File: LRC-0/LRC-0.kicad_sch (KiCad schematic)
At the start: 57 parts, among them J1 USB_C_Receptacle_USB2.0_14P, J2 Battery, J3 SMA, J4 u.FL, J5 Conn_01x08, SW1 EN, SW2 BOOT, U2 AP7361C-33E, U3 TVS1400DRV, U4 BQ24075RGT, U5 ESP32-C6-MINI-1, U6 SX1262IMLTRT, U7 BGS12WN6E6327, U8 BGS12WN6E6327, Y1 TX32-33015S-32.000-X-R

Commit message: most footprints + new rf switch (lowkey might switch back), peripherals
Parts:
- removed J5: Conn_01x08, symbol Connector_Generic:Conn_01x08
- removed U7, U8: BGS12WN6E6327, Package_LGA:Infineon_PG-TSNP-6-10_0.7x1.1mm_0.7x1.1mm_P0.4mm, symbol RF_Switch:BGS12WN6E6327
- added C22, C23: 100n, Capacitor_SMD:C_0402_1005Metric, symbol Device:C
- added J5: SPI Display, Connector_PinHeader_2.54mm:PinHeader_1x04_P2.54mm_Vertical, symbol Connector_Generic:Conn_01x04
- added R10, R17, R18, R19: 10k, Resistor_SMD:R_0402_1005Metric, symbol Device:R
- added SW3: RotaryEncoder, symbol Device:RotaryEncoder
- added SW4: 1, Button_Switch_SMD:SW_Push_SPST_NO_Alps_SKRK, symbol Switch:SW_Push
- added SW5: 0, Button_Switch_SMD:SW_Push_SPST_NO_Alps_SKRK, symbol Switch:SW_Push
- added U1, U8: RFSW1012TR7, Package_DFN_QFN:LQFN-12-1EP_2x2mm_P0.5mm_EP0.7x0.7mm, symbol RFSW1012:RFSW1012TR7
- C16: value 1u -> 470n
- C19, C20, C21: footprint (none) -> Capacitor_SMD:C_0402_1005Metric
- J1: footprint (none) -> Connector_USB:USB_C_Receptacle_GCT_USB4105-xx-A_16P_TopMnt_Horizontal
- J2: footprint (none) -> Connector_PinHeader_2.54mm:PinHeader_1x02_P2.54mm_Vertical
- J3: footprint (none) -> Connector_Coaxial:SMA_Amphenol_132289_EdgeMount
- J4: footprint (none) -> Connector_Coaxial:U.FL_Hirose_U.FL-R-SMT-1_Vertical
- R16: footprint (none) -> Resistor_SMD:R_0402_1005Metric
- SW1, SW2: footprint (none) -> Button_Switch_SMD:SW_Push_SPST_NO_Alps_SKRK
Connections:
- net +3V3: now also R10.1, R17.1, R18.1, R19.1, U1.9 (VDD), U8.9 (VDD)
- net ANT1: now also U8.5 (RF1)
- net ANT2: now also U8.11 (RF2)
- net ANT_CTRL: now also U8.7 (CTRL)
- net GND: now also C22.2, C23.2, SW4.2, SW5.2, U1.1 (GND), U1.10 (GND), U1.12 (GND), U1.3 (GND), U1.4 (GND), U1.6 (GND), U8.1 (GND), U8.10 (GND), U8.12 (GND), U8.3 (GND), U8.4 (GND), U8.6 (GND)
- net IO0: now also J5.1 (Pin_1)
- net IO1: now also J5.2 (Pin_2)
- net IO2: now also J5.3 (Pin_3)
- net IO3: now also J5.4 (Pin_4)
- net IO4: now also SW3.A
- net IO5: now also SW3.C
- net IO6: now also SW3.B
- net IO7: now also C23.1, R19.2, SW4.1
- net IO8: now also C22.1, R18.2, SW5.1
- net RF1: now also U1.5 (RF1)
- net RF2: now also U1.11 (RF2)
- net RFIN_A: now also U8.2 (RFC)
- net at R16.2: now also U1.7 (CTRL)
- net at C19.2: now also U1.2 (RFC)
- new net: R17.2, U8.8 (EN)
- new net: R10.2, U1.8 (EN)
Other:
- note removed: "GPIO"
- moved on the sheet: C19, C20, C21, FL1, J3, J4, R16

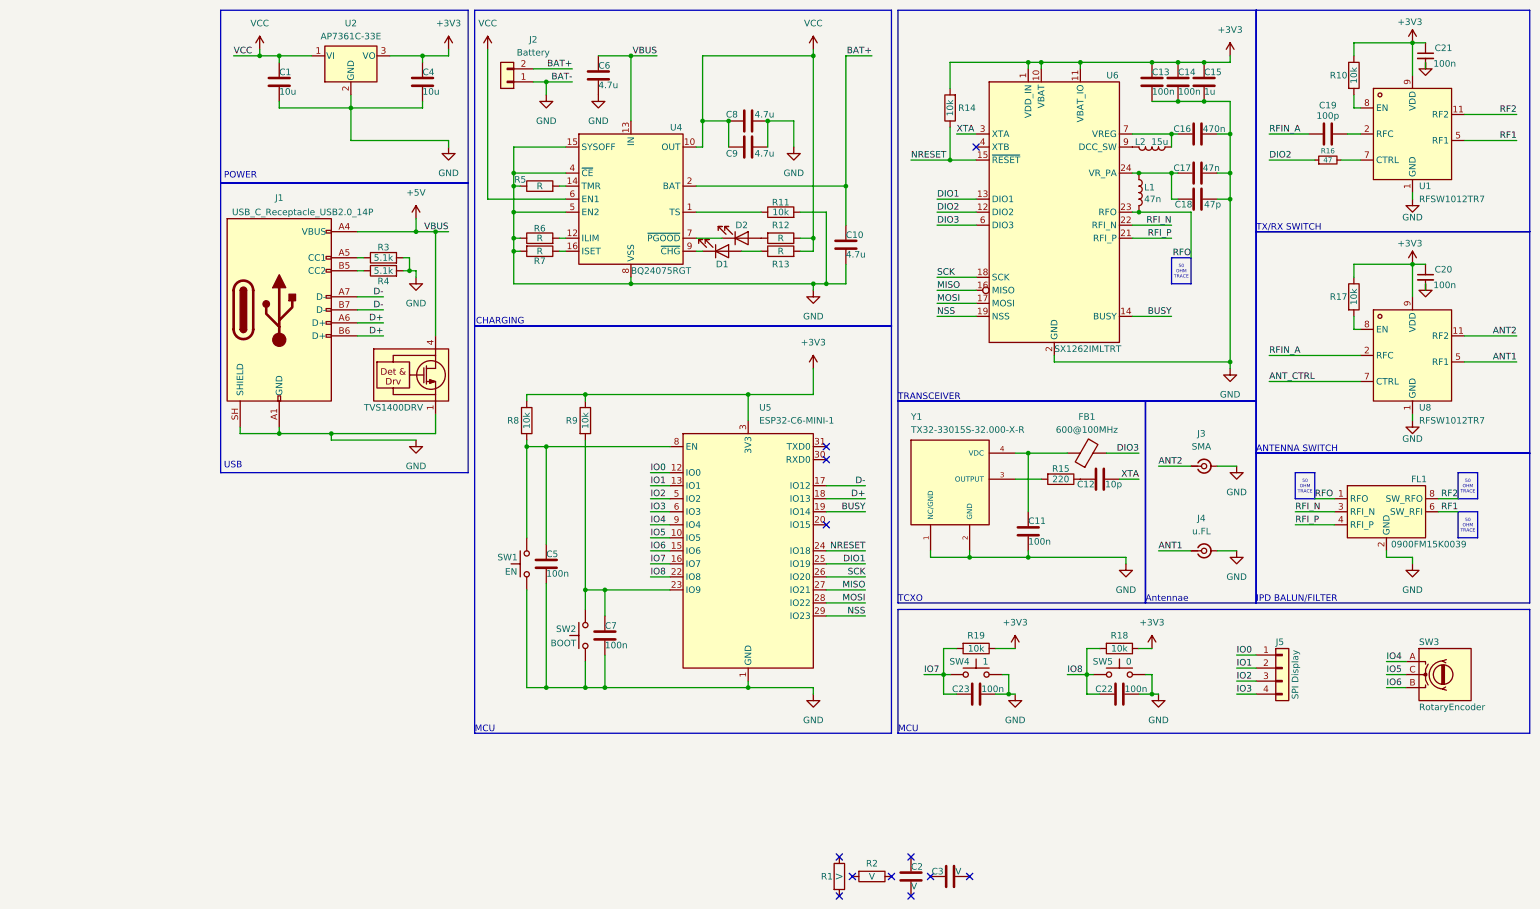
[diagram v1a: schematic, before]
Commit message: battery charger ic fix + peripherals
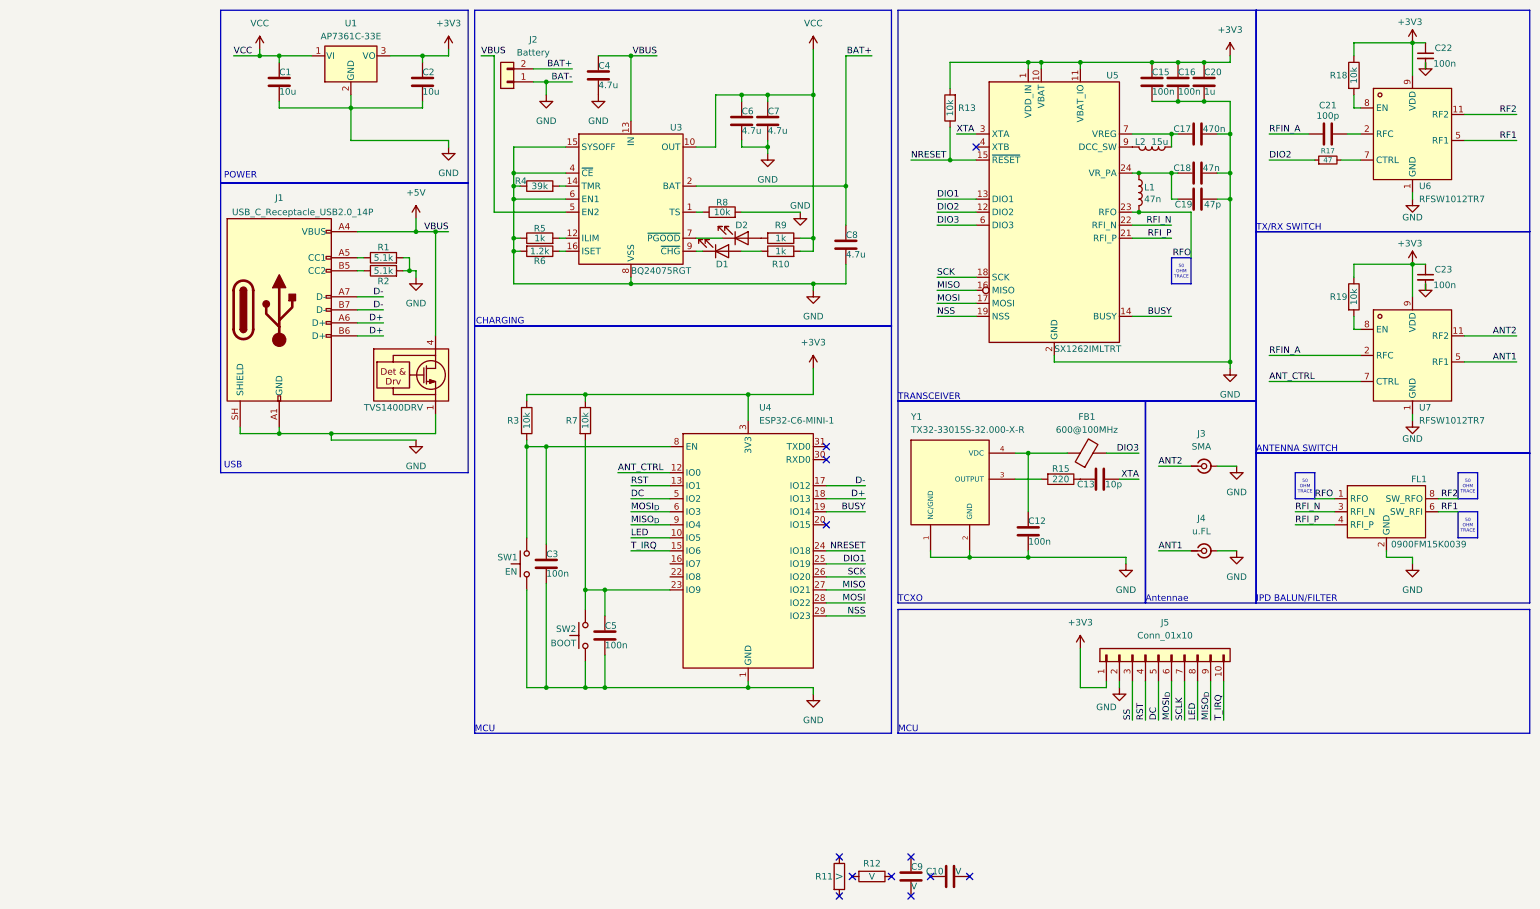
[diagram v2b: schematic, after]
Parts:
- removed C22, C23: 100n, Capacitor_SMD:C_0402_1005Metric, symbol Device:C
- removed C8, C9: 4.7u, Capacitor_SMD:C_0402_1005Metric, symbol Device:C
- removed J5: SPI Display, Connector_PinHeader_2.54mm:PinHeader_1x04_P2.54mm_Vertical, symbol Connector_Generic:Conn_01x04
- removed R11, R18, R19: 10k, Resistor_SMD:R_0402_1005Metric, symbol Device:R
- removed R5: R, Resistor_SMD:R_0402_1005Metric, symbol Device:R
- removed SW3: RotaryEncoder, symbol Device:RotaryEncoder
- removed SW4: 1, Button_Switch_SMD:SW_Push_SPST_NO_Alps_SKRK, symbol Switch:SW_Push
- removed SW5: 0, Button_Switch_SMD:SW_Push_SPST_NO_Alps_SKRK, symbol Switch:SW_Push
- added C6, C7: 4.7u, Capacitor_SMD:C_0402_1005Metric, symbol Device:C
- added J5: Conn_01x10, symbol Connector_Generic:Conn_01x10
- added R4: 39k, Resistor_SMD:R_0402_1005Metric, symbol Device:R
- added R8: 10k, Resistor_SMD:R_0402_1005Metric, symbol Device:R
- R10: renamed from R13; value R -> 1k
- R5: renamed from R6; value R -> 1k
- R6: renamed from R7; value R -> 1.2k
- R9: renamed from R12; value R -> 1k
- U4: renamed from U5; footprint RF_Module:ESP32-C6-MINI-1 -> RF_Module:ESP32-S3-WROOM-1
- renumbered C3 to C10, C11 to C12, C12 to C13, C13 to C15, C14 to C16, C16 to C17, C17 to C18, C18 to C19, C4 to C2, C15 to C20, C19 to C21, C21 to C22, C20 to C23, C5 to C3, C6 to C4, C7 to C5, C10 to C8, C2 to C9, R3 to R1, R1 to R11, R2 to R12, R14 to R13, R16 to R17, R10 to R18, R17 to R19, R4 to R2, R8 to R3, R9 to R7, U2 to U1, U3 to U2, U4 to U3, U6 to U5, U1 to U6, U8 to U7
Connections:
- net IO0 is gone; now on net ANT_CTRL: U4.12 (IO0)
- net +3V3: now also J5.1 (Pin_1)
- net +5V: now also U3.5 (EN2)
- net GND: now also U3.6 (EN1), C6.2, C7.2, J5.2 (Pin_2), R4.1, R8.2; no longer U3.5 (EN2)
- net VCC: now also C6.1, C7.1; no longer U3.6 (EN1)
- net at U3.1 (TS): now also R8.1
- net at U3.14 (TMR): now also R4.2
- net IO1 renamed RST
- net RST: now also J5.4 (Pin_4)
- net IO2 renamed DC
- net DC: now also J5.5 (Pin_5)
- net IO3 renamed MOSI_{D}
- net MOSI_{D}: now also J5.6 (Pin_6)
- net IO4 renamed MISO_{D}
- net MISO_{D}: now also J5.9 (Pin_9)
- net IO5 renamed LED
- net LED: now also J5.8 (Pin_8)
- net IO6 renamed T_IRQ
- net T_IRQ: now also J5.10 (Pin_10)
- net IO7: no longer names the net of U4.16 (IO7)
- net IO8: no longer names the net of U4.22 (IO8)
- new net SCLK: J5.7 (Pin_7)
- new net SS: J5.3 (Pin_3)

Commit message: schematic
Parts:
- D1, D2: footprint (none) -> LED_SMD:LED_0805_2012Metric
- FB1: footprint (none) -> Inductor_SMD:L_0603_1608Metric
- J5: footprint (none) -> Connector_PinHeader_2.54mm:PinHeader_1x10_P2.54mm_Vertical
- L1, L2: footprint (none) -> Inductor_SMD:L_0402_1005Metric
- U4: footprint RF_Module:ESP32-S3-WROOM-1 -> RF_Module:ESP32-C6-MINI-1
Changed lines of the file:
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@@
 			)
 		)
-		(property "Footprint" ""
+		(property "Footprint" "Inductor_SMD:L_0603_1608Metric"
 			(at 182.88 102.108 90)
 			(hide yes)
@@
 			)
 		)
-		(property "Footprint" "RF_Module:ESP32-S3-WROOM-1"
+		(property "Footprint" "RF_Module:ESP32-C6-MINI-1"
 			(at 134.62 144.78 0)
 			(hide yes)
@@
 			)
 		)
-		(property "Footprint" ""
+		(property "Footprint" "Inductor_SMD:L_0402_1005Metric"
 			(at 193.04 49.53 0)
 			(hide yes)
@@
 			)
 		)
-		(property "Footprint" ""
+		(property "Footprint" "Connector_PinHeader_2.54mm:PinHeader_1x10_P2.54mm_Vertical"
 			(at 196.85 139.7 0)
 			(hide yes)
@@
 			)
 		)
-		(property "Footprint" ""
+		(property "Footprint" "LED_SMD:LED_0805_2012Metric"
 			(at 111.76 60.96 0)
 			(hide yes)
@@
 			)
 		)
-		(property "Footprint" ""
+		(property "Footprint" "LED_SMD:LED_0805_2012Metric"
 			(at 115.57 58.42 0)
 			(hide yes)
@@
 			)
 		)
-		(property "Footprint" ""
+		(property "Footprint" "Inductor_SMD:L_0402_1005Metric"
 			(at 195.58 40.64 0)
 			(hide yes)
@@
 			"8beb553b-cd71-4e2b-a772-223167ccf878" "8e41ce3d-0b87-4755-b8d2-33e1843013d6"
 			"9afd77c0-5f47-4f9b-a946-7a0d697fb9e0" "a762f8ca-3cb3-47ad-83c8-88d4d1871ef0"
-			"b8249c6d-6442-4dcc-b269-77d21086703b" "ba0c39e8-2f22-4ef4-b4bf-0d328bdf618f"
-			"be78885b-46cc-4838-9a52-e03407f3397f" "c0b069ea-f682-487e-baeb-4ab8c4c13c54"
-			"c34ebc55-6302-44df-86b4-516ed0bf5561" "cca19fa7-7724-4027-83f7-f2765abfb53f"
-			"d84ddb03-7766-49f6-835f-c54dc88e8ff7" "dac14064-bced-4c53-b135-80ee0dbc89d7"
-			"dd5d8867-83af-4731-9750-1446e3d6ecbc" "f1fb2587-afb8-41b9-9758-8f391ef28328"
+			"b8249c6d-6442-4dcc-b269-77d21086703b" "be78885b-46cc-4838-9a52-e03407f3397f"
+			"c0b069ea-f682-487e-baeb-4ab8c4c13c54" "c34ebc55-6302-44df-86b4-516ed0bf5561"
+			"cca19fa7-7724-4027-83f7-f2765abfb53f" "d84ddb03-7766-49f6-835f-c54dc88e8ff7"
+			"dac14064-bced-4c53-b135-80ee0dbc89d7" "dd5d8867-83af-4731-9750-1446e3d6ecbc"
+			"f1fb2587-afb8-41b9-9758-8f391ef28328"
 		)
 	)

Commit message: pi filters
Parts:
- added C14, C16, C21, C24, C27: C, Capacitor_SMD:C_0402_1005Metric, symbol Device:C
- added C23: 47n, Capacitor_SMD:C_0402_1005Metric, symbol Device:C
- added L3, L4: L, Inductor_SMD:L_0402_1005Metric, symbol Device:L
- J3: renamed from J5; now not fitted
- renumbered C12 to C11, C13 to C12, C15 to C13, C16 to C15, C21 to C22, C22 to C25, C23 to C26, J3 to J4, J4 to J5, R15 to R14, R17 to R15, R18 to R16, R19 to R17
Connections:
- net ANT1: now also C14.1; no longer J5.1 (In)
- net ANT2: now also C23.1; no longer J4.1 (In)
- net DC: no longer U4.5 (IO2)
- net GND: now also C16.2, C21.2, C24.2, C27.2
- net LED: no longer U4.10 (IO5)
- net MISO_{D}: no longer U4.9 (IO4)
- net MOSI_{D}: no longer U4.6 (IO3)
- net RST: no longer U4.13 (IO1)
- net T_IRQ: no longer U4.15 (IO6)
- new net: C14.2, C16.1, L3.1
- new net: C23.2, C24.1, L4.1
- new net ANT1_{m}: C21.1, J5.1 (In), L3.2
- new net ANT2_{m}: C27.1, J4.1 (In), L4.2
- no-connect marks 12 -> 20
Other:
- note added: "Antenna Matching"
- note added: "PERIPHERALS"
- company: DUFOCKLE HOLDINGS LTD -> (none)
- title: DH/LRC-0 -> (none)

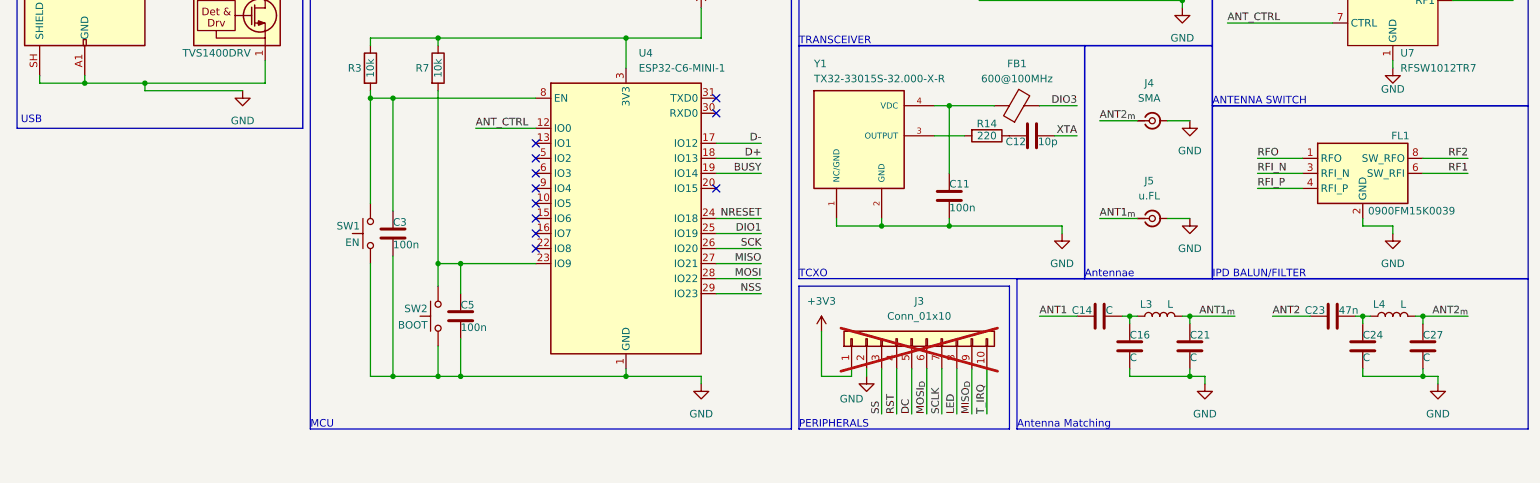
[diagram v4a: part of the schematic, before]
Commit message: removed pi filters, pcb started
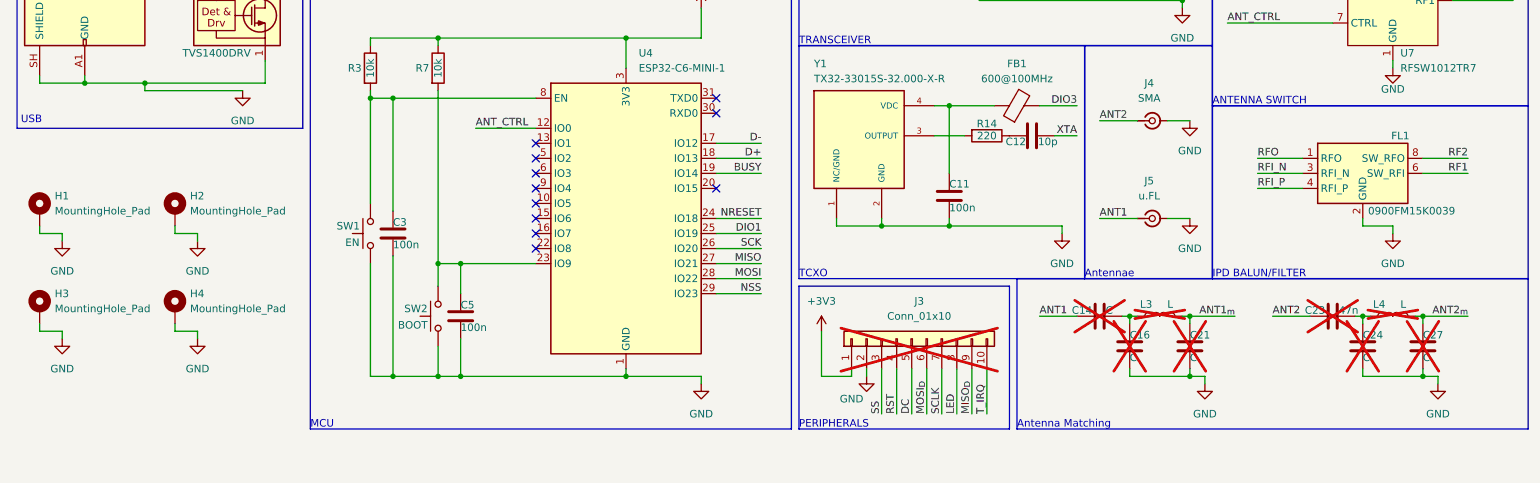
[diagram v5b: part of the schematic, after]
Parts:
- added H1, H2, H3, H4: MountingHole_Pad, MountingHole:MountingHole_3.2mm_M3, symbol Mechanical:MountingHole_Pad
- C14, C16, C21, C23, C24, C27, L3, L4: now not fitted
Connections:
- net ANT1: now also J5.1 (In)
- net ANT1_{m}: no longer J5.1 (In)
- net ANT2: now also J4.1 (In)
- net ANT2_{m}: no longer J4.1 (In)
- net GND: now also H1.1, H2.1, H3.1, H4.1

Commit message: new RF switch for pin side conflict + ground fill for some ICs
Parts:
- removed R16, R17: 10k, Resistor_SMD:R_0402_1005Metric, symbol Device:R
- removed U6, U7: RFSW1012TR7, Package_DFN_QFN:LQFN-12-1EP_2x2mm_P0.5mm_EP0.7x0.7mm, symbol RFSW1012:RFSW1012TR7
- added J6: USB_C_Receptacle_USB2.0_16P, symbol Connector:USB_C_Receptacle_USB2.0_16P
- added U6, U8: 4259-63, Package_TO_SOT_SMD:SOT-363_SC-70-6, symbol 4259_63:4259-63
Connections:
- net +3V3: now also U6.6 (VDD), U8.6 (VDD)
- net ANT1: now also U6.3 (RF2)
- net ANT2: now also U6.1 (RF1)
- net ANT_CTRL: now also U6.4 (CTRL)
- net BUSY: now also U4.28 (IO22); no longer U4.19 (IO14)
- net DIO1: now also U4.29 (IO23); no longer U4.25 (IO19)
- net GND: now also U6.2 (GND), U8.2 (GND)
- net MOSI: now also U4.26 (IO20); no longer U4.28 (IO22)
- net NSS: now also U4.19 (IO14); no longer U4.29 (IO23)
- net RF1: now also U8.3 (RF2)
- net RF2: now also U8.1 (RF1)
- net RFIN_A: now also U6.5 (RFC)
- net SCK: now also U4.25 (IO19); no longer U4.26 (IO20)
- net at R15.2: now also U8.4 (CTRL)
- net at C22.2: now also U8.5 (RFC)
- new net: J6.A1 (GND), J6.A12 (GND), J6.B1 (GND), J6.B12 (GND)
- new net: J6.A4 (VBUS), J6.A9 (VBUS), J6.B4 (VBUS), J6.B9 (VBUS)
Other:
- moved on the sheet: C22, C25, R15
